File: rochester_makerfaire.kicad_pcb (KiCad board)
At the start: 2 copper layers, 64 x 94 mm, 0 parts

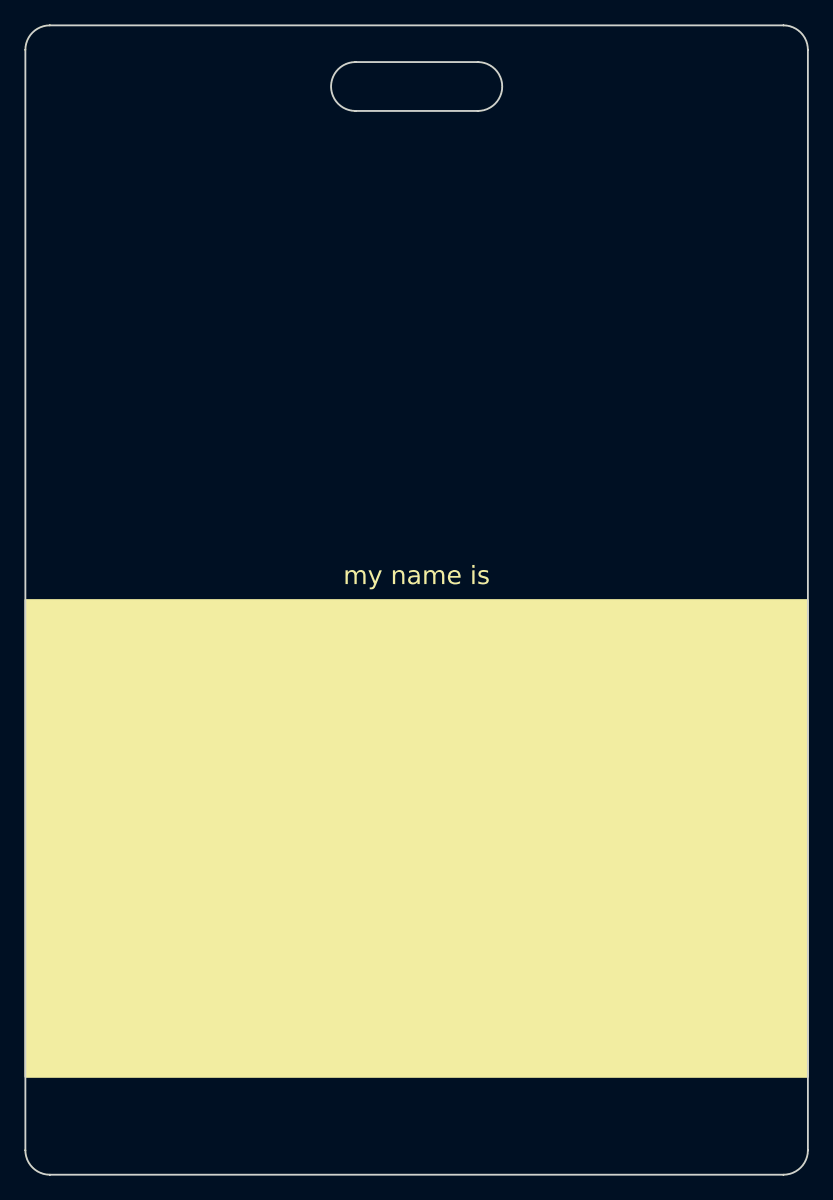
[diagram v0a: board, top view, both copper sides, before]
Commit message: First draft of the front of the badge.
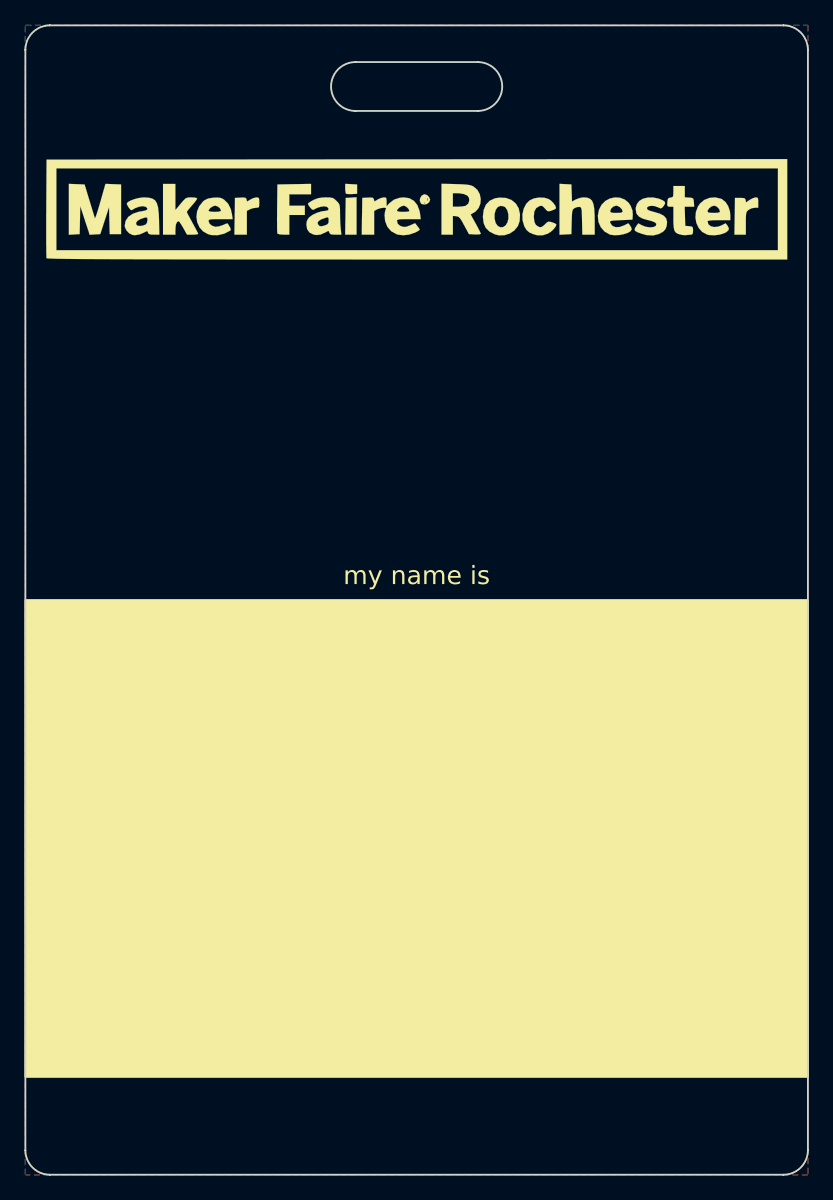
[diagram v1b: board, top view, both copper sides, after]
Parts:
- added G***: LOGO, rochester_makerfaire:maker-faire-rochester-logo2, F.Cu at (82.0, 63.0)
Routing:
- added copper zone on F.Cu, net (none)
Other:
- board text added: "Maker"

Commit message: Add 2019 deign files
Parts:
- removed the G*** at (82.0, 63.0)
- added BT1: Battery, Battery:BatteryHolder_Keystone_3001_1x12mm, B.Cu at (82.4, 72.0)
- added D1: LED, LED_THT:LED_D5.0mm, F.Cu at (105.0, 81.0)
- added D2: LED, LED_SMD:LED_1206_3216Metric, B.Cu at (82.7, 84.1)
- added D3: LED, LED_SMD:LED_0805_2012Metric, B.Cu at (83.3, 90.2)
- added D4: LED, LED_SMD:LED_0603_1608Metric, B.Cu at (64.5, 83.8)
- added D5: LED, LED_SMD:LED_0402_1005Metric, B.Cu at (64.5, 90.1)
- added G***: LOGO, rochester_makerfaire:rochester-makerspace-logo-half, F.Cu at (66.0, 135.0)
- added G***: LOGO, rochester_makerfaire:nyscate-logo, F.Cu at (97.0, 135.0)
- added G***: LOGO, rochester_makerfaire:rochester-map, B.Cu at (83.0, 98.0)
- added G***: LOGO, rochester_makerfaire:mf-robot, F.Cu at (56.0, 89.0)
- added G***: LOGO, rochester_makerfaire:thimLogo, B.Cu at (109.0, 59.0)
- added G***: LOGO, rochester_makerfaire:maker-faire-rochester-logo3, F.Cu at (82.0, 64.0)
- added G***: LOGO, rochester_makerfaire:we_are_all_makers, B.Cu at (62.0, 61.0)
- added REF**: KiCad-Logo2_8mm_SilkScreen, Symbol:KiCad-Logo2_8mm_SilkScreen, B.Cu at (100.5, 135.5)
- added REF**: OSHW-Logo2_14.6x12mm_SilkScreen, Symbol:OSHW-Logo2_14.6x12mm_SilkScreen, B.Cu at (58.0, 135.0)
- added REF**: MountingHole_2.2mm_M2_Pad, MountingHole:MountingHole_2.2mm_M2_Pad, F.Cu at (82.0, 56.5)
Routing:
- net Net-(BT1-Pad1): track 0.00 -> 101.2 mm
- net Net-(BT1-Pad2): track 0.00 -> 74.4 mm
- added copper zone on B.Cu, net Net-(BT1-Pad1)
- added copper zone on F.Cu, net Net-(BT1-Pad2)
- removed copper zone on F.Cu, net (none)
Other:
- board text added: "+"
- board text added: "-"
- board text added: "Design files and instructions at www.thimble.io/RMF2019"
- board text added: "Designed by: www.thimble.io Curriculum & kits Learn electronics!"
- board text added: "I like to Make"
- board text added: "LED 0402"
- board text added: "LED 0603"
- board text added: "LED 0805"
- board text added: "LED 1206"
- board text added: "www.rocmakers.org"
- board text removed: "my name is"
